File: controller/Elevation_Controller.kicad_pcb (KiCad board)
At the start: 4 copper layers, 120 x 200 mm, 166 parts, among them J30 TSW-115-07-S-D, J31 TSW-110-07-S-D, J401 74990111217 WE-RJ45 LAN, J501 USB4105-GF-A-120, J601 FTSH-107-01-L-DV-K, SW1 PTS636SK25SMTR LFS, SW2 PTS636SK25SMTR LFS, U1 STM32H723ZGT6, U101 TPS259470ARPWR, U202 LMR33630ADDAR, U401 LAN8742AI-CZ-TR, U402 TPS3808G30DBVR, U403 TPD4E05U06DQAR, U501 TPD2EUSB30ADRTR, U601 TPD4E05U06DQAR, U602 TPD2EUSB30ADRTR, U902 TPS3852G33DRBR, Y1 ECS-80-8-33Q-JES-TR, Y2 32.768kHz DNP, Y401 ABM8N-25.0000MHZ-8-D1X-T3

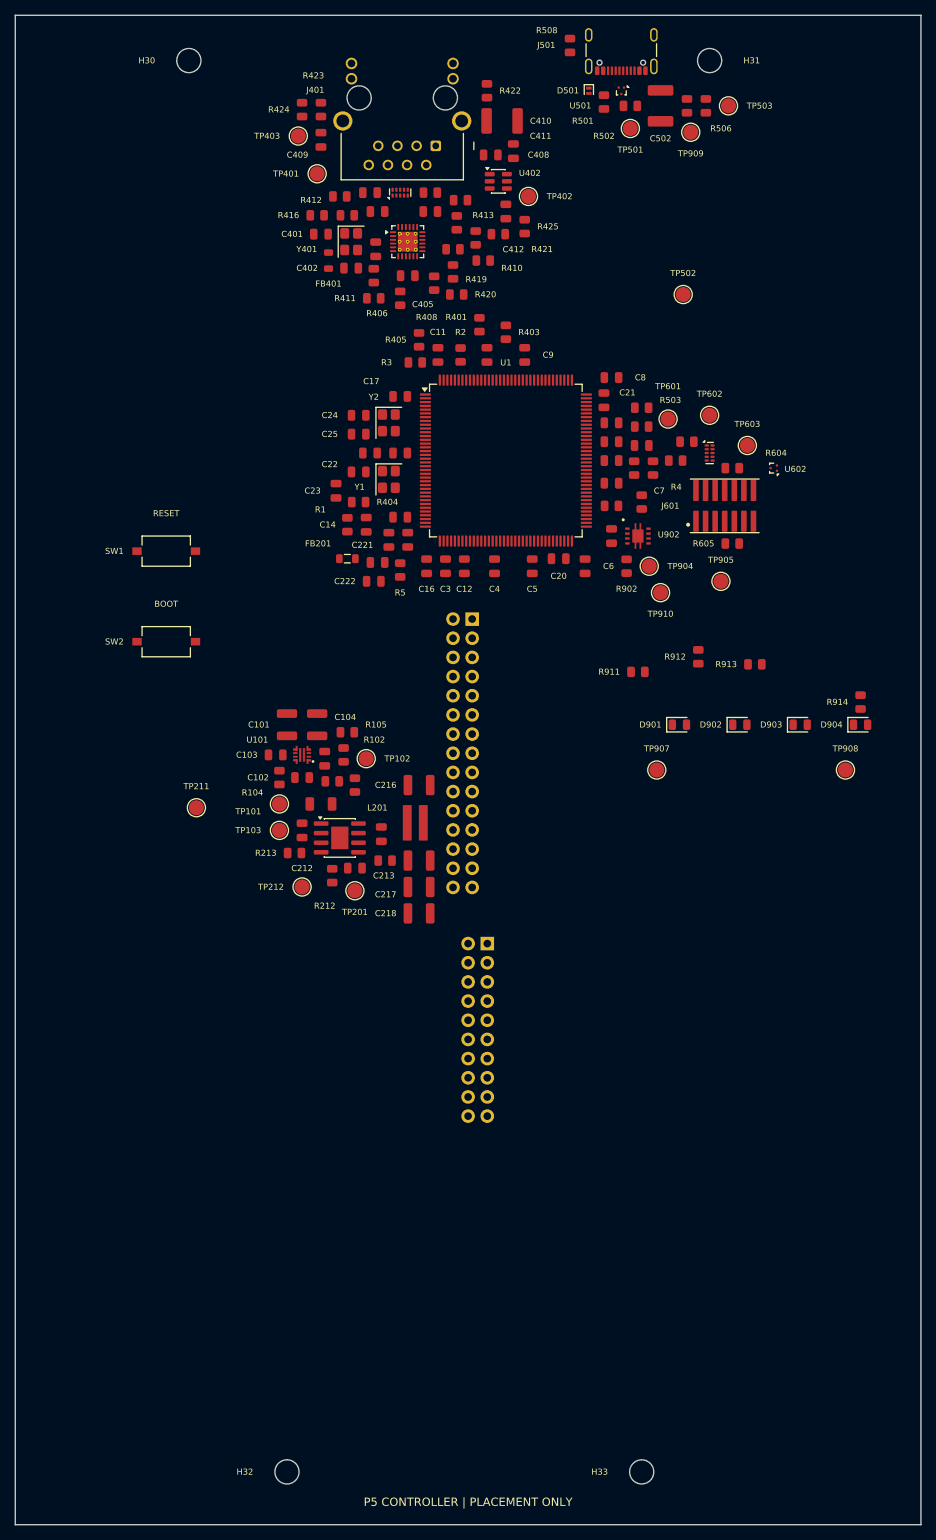
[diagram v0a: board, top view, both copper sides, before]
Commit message: Build P6 80x130 stack with redistributed SSI and stepper interfaces
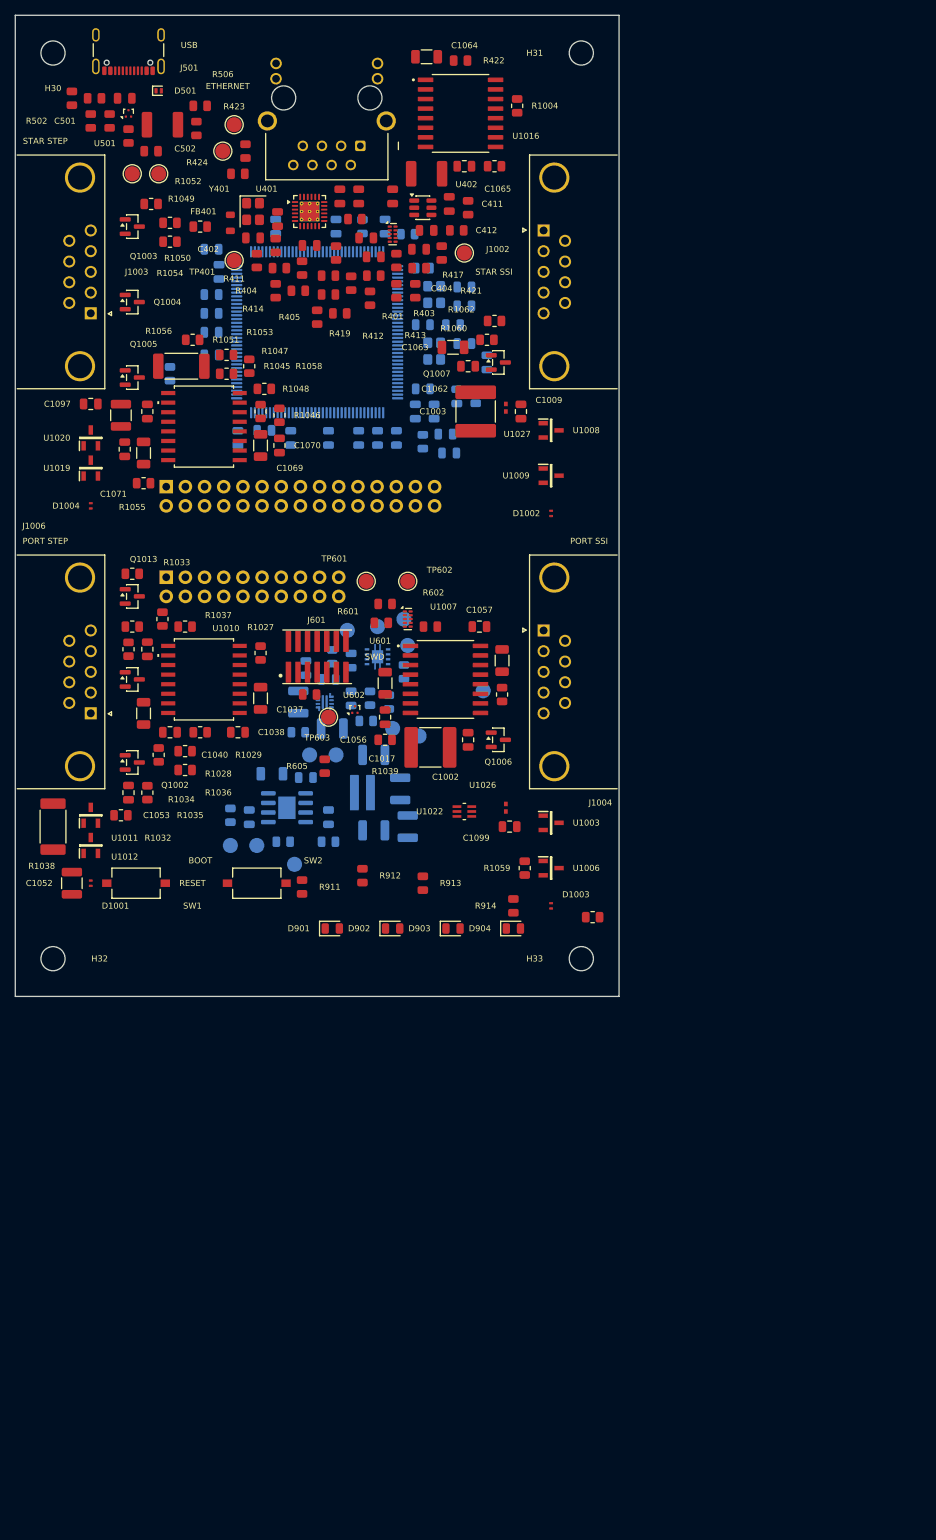
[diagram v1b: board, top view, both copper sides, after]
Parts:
- added C1002: 0.1uF, Field_Capacitor_SMD:C_0805_2012Metric, F.Cu at (80.0, 116.0)
- added C1003: 10uF, Field_Capacitor_SMD:C_2220_5750Metric, F.Cu at (81.0, 72.5)
- added C1006: 1uF, Field_Capacitor_SMD:C_1206_3216Metric, F.Cu at (69.0, 108.5)
- added C1009: 0.1uF, Field_Capacitor_SMD:C_0805_2012Metric, F.Cu at (87.0, 72.5)
- added C1017: 10uF, Field_Capacitor_SMD:C_2220_5750Metric, F.Cu at (75.0, 117.0)
- added C1037: 1uF, Field_Capacitor_SMD:C_1206_3216Metric, F.Cu at (52.5, 110.5)
- added C1038: 0.1uF, Field_Capacitor_SMD:C_0805_2012Metric, F.Cu at (49.5, 115.0)
- added C1040: 0.1uF, Field_Capacitor_SMD:C_0805_2012Metric, F.Cu at (40.5, 115.0)
- added C1042: 1uF, Field_Capacitor_SMD:C_1206_3216Metric, F.Cu at (37.0, 112.5)
- added C1051: 10nF, Field_Capacitor_SMD:C_0805_2012Metric, F.Cu at (37.5, 104.0)
- added C1052: 4.7uF, Field_Capacitor_SMD:C_1210_3225Metric, F.Cu at (27.5, 135.0)
- added C1053: 0.1uF, Field_Capacitor_SMD:C_0805_2012Metric, F.Cu at (35.0, 123.0)
- added C1056: 0.1uF, Field_Capacitor_SMD:C_0805_2012Metric, F.Cu at (69.0, 113.0)
- added C1057: 0.1uF, Field_Capacitor_SMD:C_0805_2012Metric, F.Cu at (81.5, 101.0)
- added C1058: 1uF, Field_Capacitor_SMD:C_1206_3216Metric, F.Cu at (84.5, 105.5)
- added C1062: 0.1uF, Field_Capacitor_SMD:C_0805_2012Metric, F.Cu at (80.0, 66.5)
- added C1063: 1uF, Field_Capacitor_SMD:C_1206_3216Metric, F.Cu at (78.0, 64.0)
- added C1064: 1uF, Field_Capacitor_SMD:C_1206_3216Metric, F.Cu at (74.5, 25.5)
- added C1065: 0.1uF, Field_Capacitor_SMD:C_0805_2012Metric, F.Cu at (79.5, 40.0)
- added C1069: 1uF, Field_Capacitor_SMD:C_1206_3216Metric, F.Cu at (52.5, 77.0)
- added C1070: 0.1uF, Field_Capacitor_SMD:C_0805_2012Metric, F.Cu at (55.0, 77.0)
- added C1071: 0.1uF, Field_Capacitor_SMD:C_0805_2012Metric, F.Cu at (34.5, 77.5)
- added C1072: 1uF, Field_Capacitor_SMD:C_1206_3216Metric, F.Cu at (37.0, 78.0)
- added C1096: 10nF, Field_Capacitor_SMD:C_0805_2012Metric, F.Cu at (37.5, 72.5)
- added C1097: 0.1uF, Field_Capacitor_SMD:C_0805_2012Metric, F.Cu at (30.0, 71.5)
- added C1098: 4.7uF, Field_Capacitor_SMD:C_1210_3225Metric, F.Cu at (34.0, 73.0)
- added C1099: 0.1uF, Field_Capacitor_SMD:C_0805_2012Metric, F.Cu at (85.5, 127.5)
- added D1001: TPD1E10B06DPYR, Field_TPD1E10B06DPYR:TPD1E10B06DPYR, F.Cu at (30.0, 135.0)
- added D1002: TPD1E10B06DPYR, Field_TPD1E10B06DPYR:TPD1E10B06DPYR, F.Cu at (91.0, 86.0)
- added D1003: TPD1E10B06DPYR, Field_TPD1E10B06DPYR:TPD1E10B06DPYR, F.Cu at (91.0, 138.0)
- added D1004: TPD1E10B06DPYR, Field_TPD1E10B06DPYR:TPD1E10B06DPYR, F.Cu at (30.0, 85.0)
- added J1002: DE9_Socket_MountingHoles, Field_Connector_Dsub:DSUB-9_Socket_Horizontal_P2.77x2.84mm_EdgePinOffset7.70mm_Housed_MountingHolesOffset9.12mm, F.Cu at (90.0, 48.5)
- added J1003: DE9_Socket_MountingHoles, Field_Connector_Dsub:DSUB-9_Socket_Horizontal_P2.77x2.84mm_EdgePinOffset7.70mm_Housed_MountingHolesOffset9.12mm, F.Cu at (30.0, 59.5)
- added J1004: DE9_Socket_MountingHoles, Field_Connector_Dsub:DSUB-9_Socket_Horizontal_P2.77x2.84mm_EdgePinOffset7.70mm_Housed_MountingHolesOffset9.12mm, F.Cu at (90.0, 101.5)
- added J1006: DE9_Socket_MountingHoles, Field_Connector_Dsub:DSUB-9_Socket_Horizontal_P2.77x2.84mm_EdgePinOffset7.70mm_Housed_MountingHolesOffset9.12mm, F.Cu at (30.0, 112.5)
- added Q1001: 2N7002KQ-7, Field_Package_TO_SOT_SMD:SOT-23, F.Cu at (35.5, 108.0)
- added Q1002: 2N7002KQ-7, Field_Package_TO_SOT_SMD:SOT-23, F.Cu at (35.5, 119.0)
- added Q1003: 2N7002KQ-7, Field_Package_TO_SOT_SMD:SOT-23, F.Cu at (35.5, 48.0)
- added Q1004: 2N7002KQ-7, Field_Package_TO_SOT_SMD:SOT-23, F.Cu at (35.5, 58.0)
- added Q1005: 2N7002KQ-7, Field_Package_TO_SOT_SMD:SOT-23, F.Cu at (35.5, 68.0)
- added Q1006: 2N7002KQ-7, Field_Package_TO_SOT_SMD:SOT-23, F.Cu at (84.0, 116.0)
- added Q1007: 2N7002KQ-7, Field_Package_TO_SOT_SMD:SOT-23, F.Cu at (84.0, 66.0)
- added Q1013: 2N7002KQ-7, Field_Package_TO_SOT_SMD:SOT-23, F.Cu at (35.5, 97.0)
- added R1002: 120, Field_Resistor_SMD:R_0805_2012Metric, F.Cu at (84.5, 110.0)
- added R1004: 120, Field_Resistor_SMD:R_0805_2012Metric, F.Cu at (86.5, 32.0)
- added R1027: 4.7K, Field_Resistor_SMD:R_0805_2012Metric, F.Cu at (52.5, 104.5)
- added R1028: 10K, Field_Resistor_SMD:R_0805_2012Metric, F.Cu at (42.5, 117.5)
- added R1029: 10K, Field_Resistor_SMD:R_0805_2012Metric, F.Cu at (44.5, 115.0)
- added R1030: 100, Field_Resistor_SMD:R_0805_2012Metric, F.Cu at (35.0, 104.0)
- added R1031: 100, Field_Resistor_SMD:R_0805_2012Metric, F.Cu at (35.5, 101.0)
- added R1032: 100, Field_Resistor_SMD:R_0805_2012Metric, F.Cu at (34.0, 126.0)
- added R1033: 47K, Field_Resistor_SMD:R_0805_2012Metric, F.Cu at (35.5, 94.0)
- added R1034: 47K, Field_Resistor_SMD:R_0805_2012Metric, F.Cu at (39.0, 118.0)
- added R1035: 47K, Field_Resistor_SMD:R_0805_2012Metric, F.Cu at (37.5, 123.0)
- added R1036: 10K, Field_Resistor_SMD:R_0805_2012Metric, F.Cu at (42.5, 120.0)
- added R1037: 10K, Field_Resistor_SMD:R_0805_2012Metric, F.Cu at (42.5, 101.0)
- added R1038: 10, Field_Resistor_SMD:R_2512_6332Metric_Pad1.40x3.35mm_HandSolder, F.Cu at (25.0, 127.5)
- added R1039: 10K, Field_Resistor_SMD:R_0805_2012Metric, F.Cu at (69.0, 116.0)
- added R1040: 10K, Field_Resistor_SMD:R_0805_2012Metric, F.Cu at (83.5, 40.0)
- added R1045: 10K, Field_Resistor_SMD:R_0805_2012Metric, F.Cu at (51.0, 66.5)
- added R1046: 10K, Field_Resistor_SMD:R_0805_2012Metric, F.Cu at (55.0, 73.0)
- added R1047: 10K, Field_Resistor_SMD:R_0805_2012Metric, F.Cu at (48.0, 67.5)
- added R1048: 10K, Field_Resistor_SMD:R_0805_2012Metric, F.Cu at (52.5, 72.5)
- added R1049: 100, Field_Resistor_SMD:R_0805_2012Metric, F.Cu at (40.5, 47.5)
- added R1050: 100, Field_Resistor_SMD:R_0805_2012Metric, F.Cu at (44.5, 48.0)
- added R1051: 100, Field_Resistor_SMD:R_0805_2012Metric, F.Cu at (43.5, 63.0)
- added R1052: 47K, Field_Resistor_SMD:R_0805_2012Metric, F.Cu at (38.0, 45.0)
- added R1053: 47K, Field_Resistor_SMD:R_0805_2012Metric, F.Cu at (48.0, 65.0)
- added R1054: 47K, Field_Resistor_SMD:R_0805_2012Metric, F.Cu at (40.5, 50.0)
- added R1055: 4.7K, Field_Resistor_SMD:R_0805_2012Metric, F.Cu at (37.0, 82.0)
- added R1056: 10, Field_Resistor_SMD:R_2512_6332Metric_Pad1.40x3.35mm_HandSolder, F.Cu at (42.0, 66.5)
- added R1057: 10K, Field_Resistor_SMD:R_0805_2012Metric, F.Cu at (39.5, 100.0)
- added R1058: 10K, Field_Resistor_SMD:R_0805_2012Metric, F.Cu at (53.0, 69.5)
- added R1059: 2.2K, Field_Resistor_SMD:R_0805_2012Metric, F.Cu at (87.5, 133.0)
- added R1060: 2.2K, Field_Resistor_SMD:R_0805_2012Metric, F.Cu at (82.5, 63.0)
- added R1061: 47K, Field_Resistor_SMD:R_0805_2012Metric, F.Cu at (96.5, 139.5)
- added R1062: 47K, Field_Resistor_SMD:R_0805_2012Metric, F.Cu at (83.5, 60.5)
- added U1003: TPD2E2U06QDBZRQ1, Field_TPD2E2U06QDBZRQ1:SOT95P237X95-3N, F.Cu at (91.0, 127.0)
- added U1006: TPD2E2U06QDBZRQ1, Field_TPD2E2U06QDBZRQ1:SOT95P237X95-3N, F.Cu at (91.0, 133.0)
- added U1007: ISO1432DWR, Field_ISO1432DWR:ISO1432DWR, F.Cu at (77.0, 108.0)
- added U1008: TPD2E2U06QDBZRQ1, Field_TPD2E2U06QDBZRQ1:SOT95P237X95-3N, F.Cu at (91.0, 75.0)
- added U1009: TPD2E2U06QDBZRQ1, Field_TPD2E2U06QDBZRQ1:SOT95P237X95-3N, F.Cu at (91.0, 81.0)
- added U1010: ISO6762DWR, Field_ISO6762QDWRQ1:ISO6762QDWRQ1, F.Cu at (45.0, 108.0)
- added U1011: TPD2E2U06QDBZRQ1, Field_TPD2E2U06QDBZRQ1:SOT95P237X95-3N, F.Cu at (30.0, 126.0)
- added U1012: TPD2E2U06QDBZRQ1, Field_TPD2E2U06QDBZRQ1:SOT95P237X95-3N, F.Cu at (30.0, 130.0)
- added U1016: ISO1432DWR, Field_ISO1432DWR:ISO1432DWR, F.Cu at (79.0, 33.0)
- added U1018: ISO6762DWR, Field_ISO6762QDWRQ1:ISO6762QDWRQ1, F.Cu at (45.0, 74.5)
- added U1019: TPD2E2U06QDBZRQ1, Field_TPD2E2U06QDBZRQ1:SOT95P237X95-3N, F.Cu at (30.0, 80.0)
- added U1020: TPD2E2U06QDBZRQ1, Field_TPD2E2U06QDBZRQ1:SOT95P237X95-3N, F.Cu at (30.0, 76.0)
- added U1022: SN74LVC2G07DCKR(UMW), Field_SN74LVC2G07:SN74LVC2G07, F.Cu at (79.5, 125.5)
- added U1026: TPD1E10B09DPYR, Field_TPD1E10B09DPYR:TPD1E10B09DPYR, F.Cu at (85.0, 125.0)
- added U1027: TPD1E10B09DPYR, Field_TPD1E10B09DPYR:TPD1E10B09DPYR, F.Cu at (85.0, 72.0)
- C1, C10, C101, C102, C103, C104, C105, C11, C12, C13, C14, C15, C16, C17, C18, C19, C2, C20, C21, C211, C212, C213, C214, C215, C216, C217, C218, C22, C221, C222, C23, C24, C25, C26, C27, C3, C4, C5, C6, C7, C8, C9, C902, FB201, L201, R1, R101, R102, R103, R104, R105, R2, R211, R212, R213, R3, R4, R5, R902, TP101, TP102, TP103, TP201, TP211, TP212, TP904, TP905, TP907, TP908, TP909, TP910, U1, U101, U202, U902, Y1, Y2: moved to B.Cu
- moved R504 84.5 mm to (30.5, 31.0)
- moved C501 82.5 mm to (34.5, 31.0)
- moved R503 80.1 mm to (32.5, 34.0), turned to -90 degrees
- moved R507 78.7 mm to (38.0, 38.0), turned to 0 degrees
- moved TP909 77.5 mm to (68.0, 101.0)
- moved TP502 74.7 mm to (35.5, 41.0)
- moved H32 74.7 mm to (25.0, 145.0)
- moved TP908 68.5 mm to (64.0, 101.5)
- moved H33 68.5 mm to (95.0, 145.0)
- moved R502 68.0 mm to (30.0, 34.0), turned to 90 degrees
- moved R506 67.0 mm to (44.5, 32.0), turned to 180 degrees
- moved R501 66.6 mm to (35.0, 36.0), turned to 90 degrees
- moved R508 66.4 mm to (27.5, 31.0)
- moved TP603 66.2 mm to (61.5, 113.0)
- moved C502 66.0 mm to (39.5, 34.5), turned to 180 degrees
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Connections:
- J30 pad 10: STAR_STR8_FAULT -> STAR_ENC_A
- J30 pad 11: GND -> STAR_ENC_B
- J30 pad 12: GND -> STAR_ENC_Z
- J30 pad 13: PORT_SSI_CLK -> GND
- J30 pad 14: STAR_SSI_CLK -> GND
- J30 pad 15: PORT_SSI_DATA -> STM32_SCL
- J30 pad 16: STAR_SSI_DATA -> STM32_SDA
- J30 pad 17: PORT_ENC_PRESET_N -> TX_CAN
- J30 pad 18: STAR_ENC_PRESET_N -> RX_CAN
- J30 pad 19: PORT_BRAKE_RELEASE_CMD -> Silent_Mode
- J30 pad 20: STAR_BRAKE_RELEASE_CMD -> PIVOT_MODBUS_TX
- J30 pad 21: GND -> PIVOT_MODBUS_RX
- J30 pad 22: GND -> PIVOT_MODBUS_DE
- J30 pad 23: HOME_POS -> NRST
- J30 pad 24: E_STOP_OK -> GND
- J30 pad 27: GND -> 3V3_DIG
- J30 pad 28: GND -> 3V3_DIG
- J30 pad 29: 3V3_DIG -> GND
- J30 pad 3: PORT_STR8_STEP_CMD -> PORT_BRAKE_RELEASE_CMD
- J30 pad 30: 3V3_DIG -> GND
- J30 pad 4: STAR_STR8_STEP_CMD -> STAR_BRAKE_RELEASE_CMD
- J30 pad 5: PORT_STR8_DIR_CMD -> HOME_POS
- J30 pad 6: STAR_STR8_DIR_CMD -> E_STOP_OK
- J30 pad 7: PORT_STR8_DISABLE -> PORT_ENC_A
- J30 pad 8: STAR_STR8_DISABLE -> PORT_ENC_B
- J30 pad 9: PORT_STR8_FAULT -> PORT_ENC_Z
- J31 pad 1: PORT_ENC_A -> -BATT
- J31 pad 10: GND -> +6.5V_ENC_PORT
- J31 pad 11: STM32_SCL -> +5V_ENC_PORT
- J31 pad 12: STM32_SDA -> +5V_ENC_PORT
- J31 pad 13: PIVOT_MODBUS_TX -> -BATT
- J31 pad 14: PIVOT_MODBUS_RX -> -BATT
- J31 pad 15: TX_CAN -> +6.5V_ENC_STAR
- J31 pad 16: RX_CAN -> +6.5V_ENC_STAR
- J31 pad 17: Silent_Mode -> +5V_ENC_STAR
- J31 pad 18: PIVOT_MODBUS_DE -> +5V_ENC_STAR
- J31 pad 19: NRST -> -BATT
- J31 pad 2: PORT_ENC_B -> -BATT
- J31 pad 20: GND -> -BATT
- J31 pad 3: GND -> -BATT
- J31 pad 4: GND -> -BATT
- J31 pad 5: STAR_ENC_A -> +5V_FIELD
- J31 pad 6: STAR_ENC_B -> +5V_FIELD
- J31 pad 7: PORT_ENC_Z -> -BATT
- J31 pad 8: STAR_ENC_Z -> -BATT
- J31 pad 9: GND -> +6.5V_ENC_PORT
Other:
- board size 120 x 200 mm -> 80 x 130 mm
- board text added: "ETHERNET"
- board text added: "J30 CLEAN"
- board text added: "J31 FIELD"
- board text added: "P6 80 x 130 | UNROUTED"
- board text added: "PORT SSI"
- board text added: "PORT STEP"
- board text added: "STAR SSI"
- board text added: "STAR STEP"
- board text added: "SWD"
- board text added: "USB"
- board text removed: "120 x 200 mm / 4 layers / NO ROUTING"
- board text removed: "OUTWARD FACE: TOP"
- board text removed: "P5 CONTROLLER | PLACEMENT ONLY"
